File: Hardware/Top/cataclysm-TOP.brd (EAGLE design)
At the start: 160 x 100 mm, 0 parts

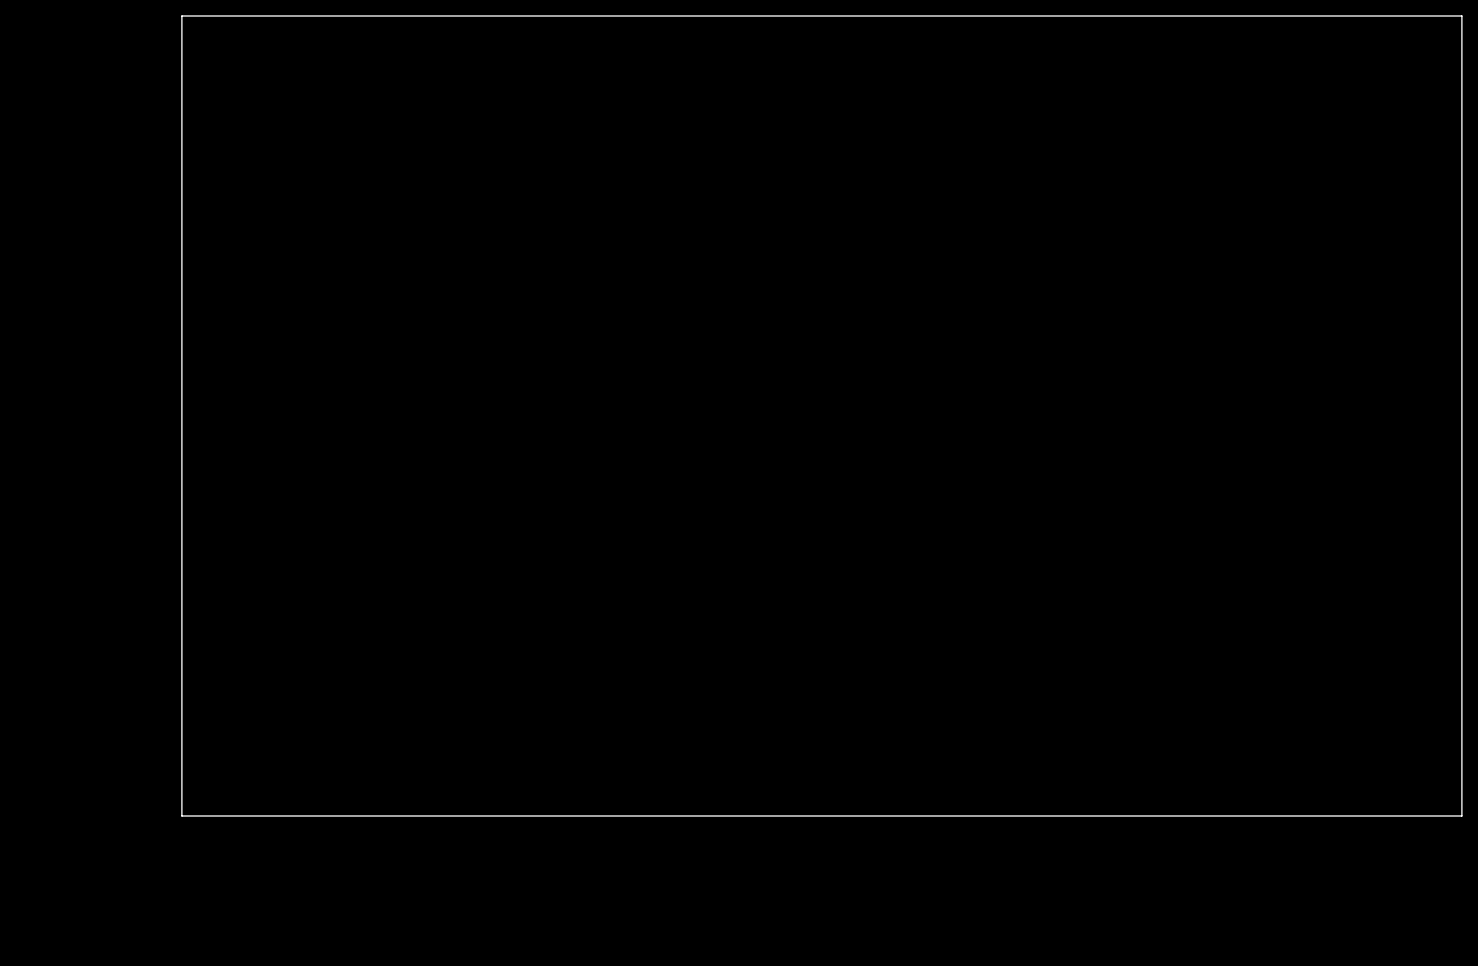
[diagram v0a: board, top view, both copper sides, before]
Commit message: Added OLED display, power management section, bluetooth microcontroller, and buttons
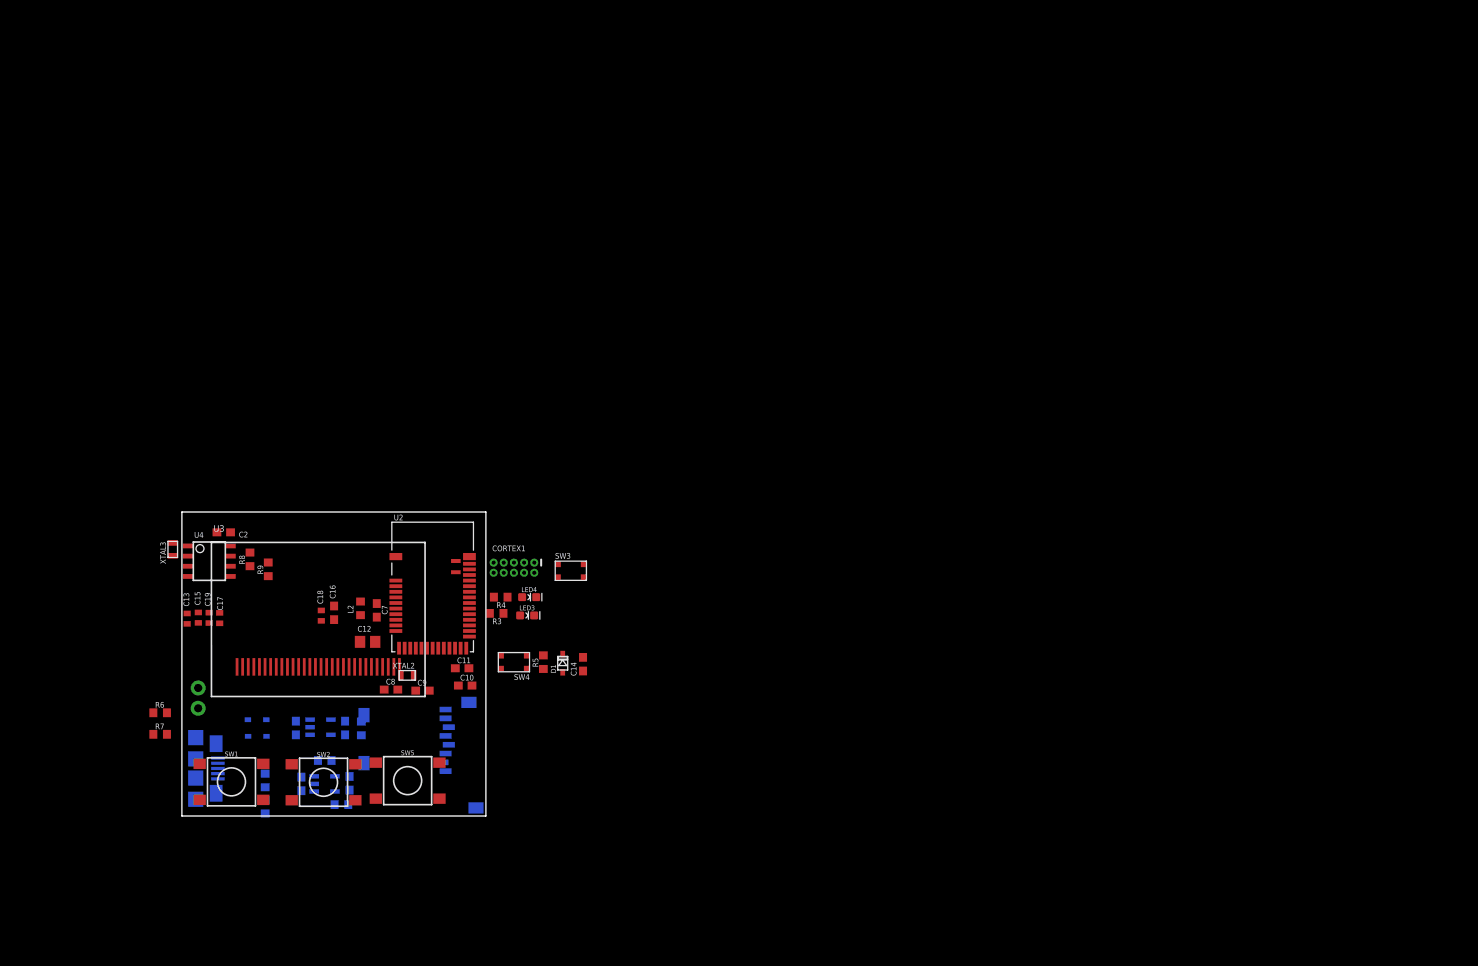
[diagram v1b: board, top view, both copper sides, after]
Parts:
- added C10, C11: 300p, LinnesLab-Passives:C0603
- added C12: 10u, LinnesLab-Passives:C0805
- added C13, C15, C17, C18, C19: 2.2uF, LinnesLab-Passives:C0402
- added C14: 100n, LinnesLab-Passives:C0603
- added C16: 10uF, LinnesLab-Passives:C0603
- added C2, C5, C6, C7: 1u, LinnesLab-Passives:C0603
- added C20, C21: 4.7u, LinnesLab-Passives:C0603
- added C8, C9: (no value), LinnesLab-Passives:C0603
- added CHRG2: MCP73831, LinnesLab-Power:SOT23-5
- added CORTEX1: CORTEX_DEBUG_PTH, LinnesLab-Connectors:2X5-PTH-1.27MM
- added D1, D4, D5: (no value), LinnesLab-DiscreteSemi:USC
- added J2: (no value), LinnesLab-Connectors:1X02
- added L2: 10u, LinnesLab-Passives:L0603
- added LDO2: MIC5504, LinnesLab-Power:SOT23-5
- added LED3: RED, LinnesLab-LED:LED-0603
- added LED4: BLUE, LinnesLab-LED:LED-0603
- added R11: (no value), LinnesLab-Passives:R0603
- added R12, R13, R14, R15: 100k, LinnesLab-Passives:R0603
- added R3, R4: 1k, LinnesLab-Passives:R0603
- added R5, R6, R8, R9: 10k, LinnesLab-Passives:R0603
- added R7: 390k, LinnesLab-Passives:R0603
- added SD3: (no value), LinnesLab-Connectors:MICROSD
- added SW1, SW2, SW5: SWITCH.MOM, LinnesLab-Switches:TACTILE_SWITCH_SMD_6.2MM_TALL
- added SW3, SW4: (no value), LinnesLab-Switches:BUTTON-GULLWING
- added U2: NRF52832_MODULE_MDBT42, LinnesLab-Microcontrollers:BLE_MODULE_RAYTAC_MDBT42
- added U3: (no value), LinnesLab-Displays:UG-2864HSWEG01_0.96IN_NO-WRAPAROUND
- added U4: PCF8523, LinnesLab-Clocks:SO8
- added USB2: USB.MICRO-BIGGERPADS, LinnesLab-Connectors:USB-MICRO-01.BIGGERPADS
- added XTAL2: 32.768kHz, LinnesLab-Clocks:2-SMD.NOLEAD.2.0MMTO1.2MM
- added XTAL3: 32.7680kHz, LinnesLab-Clocks:2-SMD.NOLEAD.2.0MMTO1.2MM
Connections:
- new net 3.3V: C12.2, C17.2, C19.2, C2.1, C6.1, CORTEX1.1, D1.-, LDO2.5, R15.2, R5.2, R8.2, R9.2, SD3.4, U2.11, U3.6, U3.9, U4.8
- new net BATT: R13.1, R14.2
- new net CD1: SD3.CD1
- new net CD2: SD3.CD2
- new net CHRG.STAT: CHRG2.1, R12.1
- new net CS.OLED: U3.13
- new net DC.OLED: U3.15
- new net DFU: SW3.3, U2.34
- new net DTR: C14.1
- new net FRST: U2.38
- new net GND: C10.2, C11.2, C12.1, C16.1, C17.1, C18.1, C19.1, C2.2, C20.2, C21.1, C5.1, C6.2, C7.2, C8.1, C9.2, CHRG2.2, CORTEX1.3, CORTEX1.5, CORTEX1.7, CORTEX1.9, J2.1, LDO2.2, LED3.C, LED4.C, R11.1, R14.1, R15.1, R6.1, R7.2, SD3.6, SD3.MT1, SD3.MT2, SW3.1, SW4.3, U2.1, U2.12, U2.24, U2.39, U3.1, U3.10, U3.12, U3.29, U3.30, U3.8, U4.4, USB2.5
- new net LED1: R3.2, U2.31
- new net LED2: R4.2, U2.33
- new net MISO: SD3.7, U2.28
- new net MOSI: SD3.3, U2.27, U3.19
- new net N$1: R6.2, U3.11
- new net N$10: LED4.A, R4.1
- new net N$11: L2.1, U2.10
- new net N$12: C7.1, L2.2, U2.9
- new net N$13: C16.2, U3.28
- new net N$14: CORTEX1.8
- new net N$15: C18.2, U3.27
- new net N$17: CHRG2.5, R11.2
- new net N$19: U4.2, XTAL3.P$1
- new net N$2: R7.1, U3.26
- new net N$20: U4.1, XTAL3.P$2
- new net N$3: C13.2, U3.2
- new net N$4: C8.2, U2.13, XTAL2.P$1
- new net N$5: C13.1, U3.3
- new net N$6: C9.1, U2.14, XTAL2.P$2
- new net N$7: C15.2, U3.4
- new net N$8: C15.1, U3.5
- new net N$9: LED3.A, R3.1
- new net P0.09/NFC1: C11.1, U2.22
- new net P0.10/NFC2: C10.1, U2.23
- new net RESET: C14.2, CORTEX1.10, D1.+, R5.1, SW4.1, U2.35
- new net RESET.OLED: U3.14
- new net RXD: U2.21
- new net SCK: SD3.5, U2.26, U3.18
- new net SCL: R8.1, U2.3, U4.6
- new net SD.CS: SD3.2
- new net SDA: R9.1, U2.2, U4.5
- new net SWCLK: CORTEX1.4, U2.36
- new net SWDIO: CORTEX1.2, U2.37
- new net SWO: CORTEX1.6, U2.32
- new net TXD: U2.19
- new net USB+: USB2.3
- new net USB-: USB2.2
- new net VBATT: U4.3
- new net VIN: C21.2, C5.2, CHRG2.4, D4.-, D5.-, LDO2.1, LDO2.3, R12.2
- new net VLIPO: C20.1, CHRG2.3, D4.+, J2.2, R13.2
- new net V_USB: D5.+, USB2.1
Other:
- board size 160 x 100 mm -> 38 x 38 mm

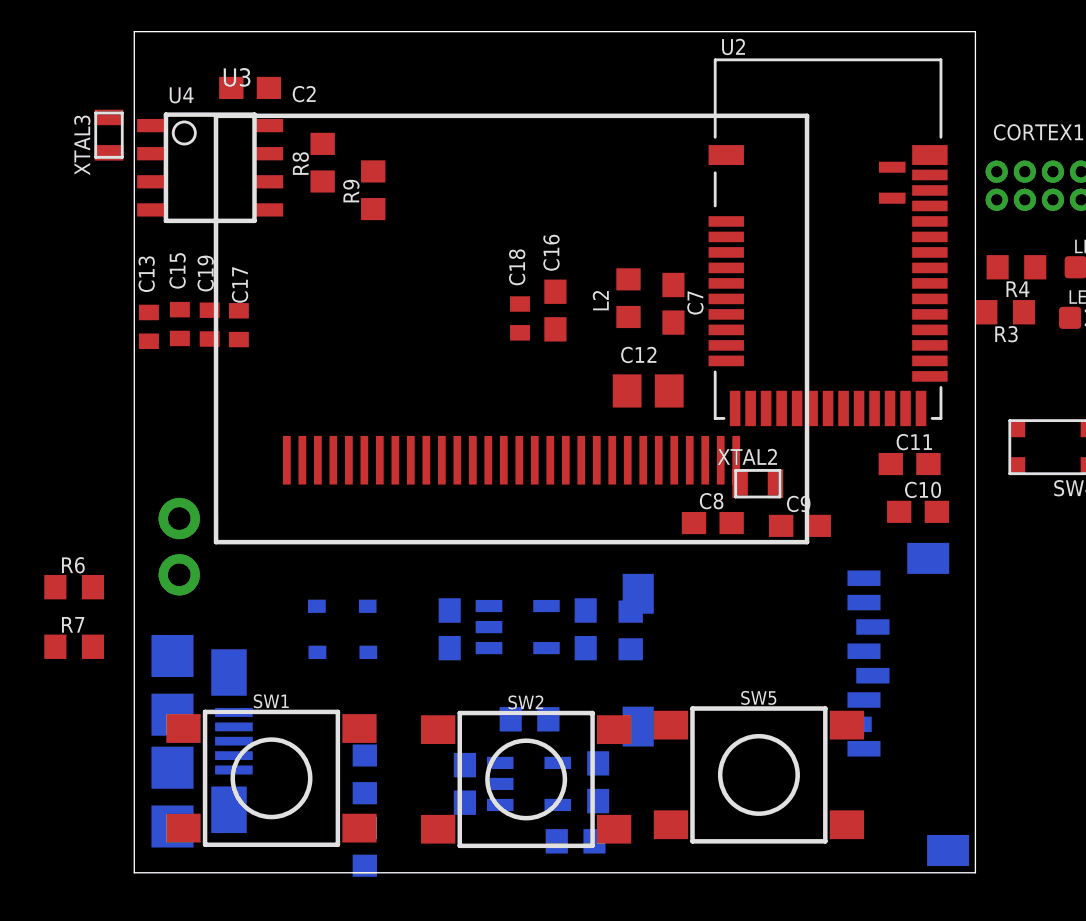
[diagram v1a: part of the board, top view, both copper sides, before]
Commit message: complete top circuit schematic
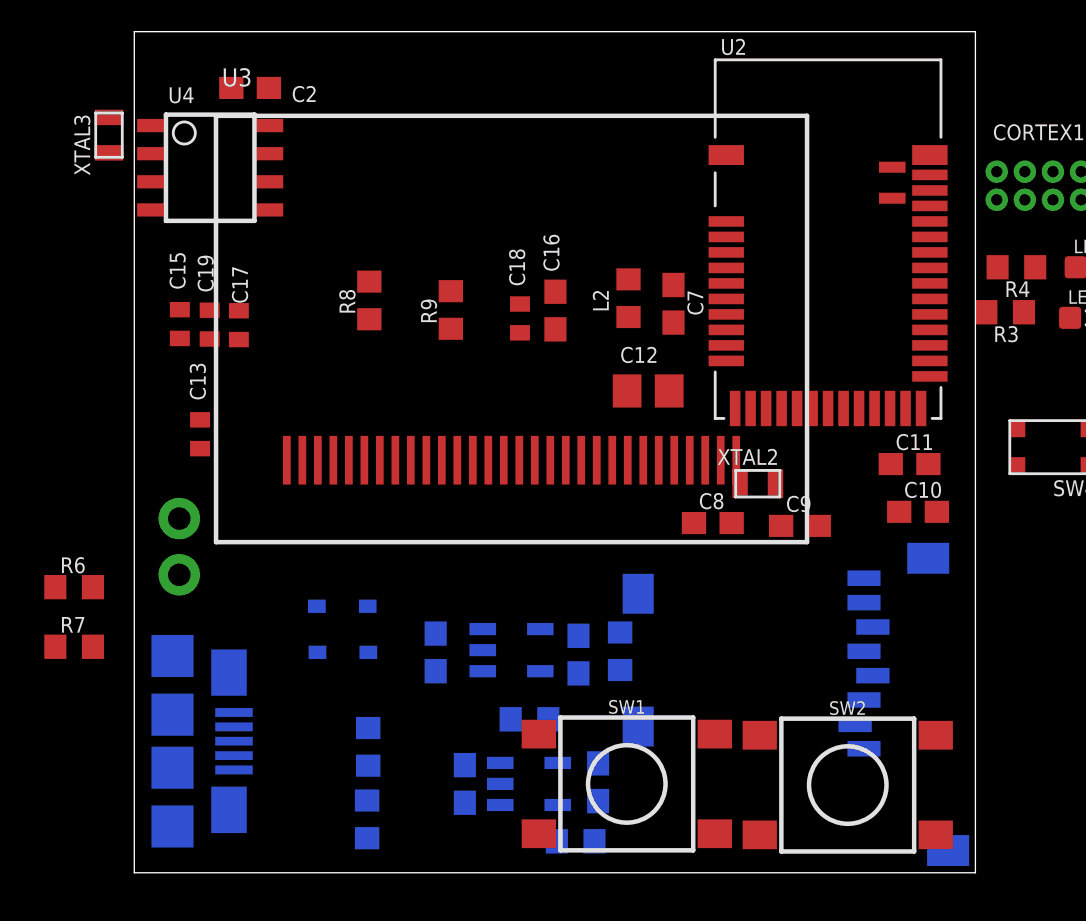
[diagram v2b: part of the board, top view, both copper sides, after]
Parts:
- removed SW5: SWITCH.MOM, LinnesLab-Switches:TACTILE_SWITCH_SMD_6.2MM_TALL
- moved SW1 16.1 mm to (22.3, 4.01)
- moved SW2 14.5 mm to (32.2, 3.96)
- moved R8 6.57 mm to (10.6, 25.9)
- moved R9 6.45 mm to (14.3, 25.4)
- moved C13 5.37 mm to (2.97, 19.8)
- moved R14 1.25 mm to (10.6, 5.69)
- moved R13 1.25 mm to (10.5, 2.41)
- moved C5 1.22 mm to (13.6, 9.96)
- moved C6 1.19 mm to (20.1, 9.86)
- moved LDO2 1.08 mm to (17.0, 10.1)
- moved R15 1.06 mm to (21.9, 10.0)
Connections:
- new net N$16: SW2.B2
- new net N$21: SW1.B2
- new net SW1: SW1.A1, SW2.A1
- net GND: now also SW1.B1, SW2.B1, USB2.S1, USB2.S2, USB2.S3, USB2.S4, USB2.S5, USB2.S6

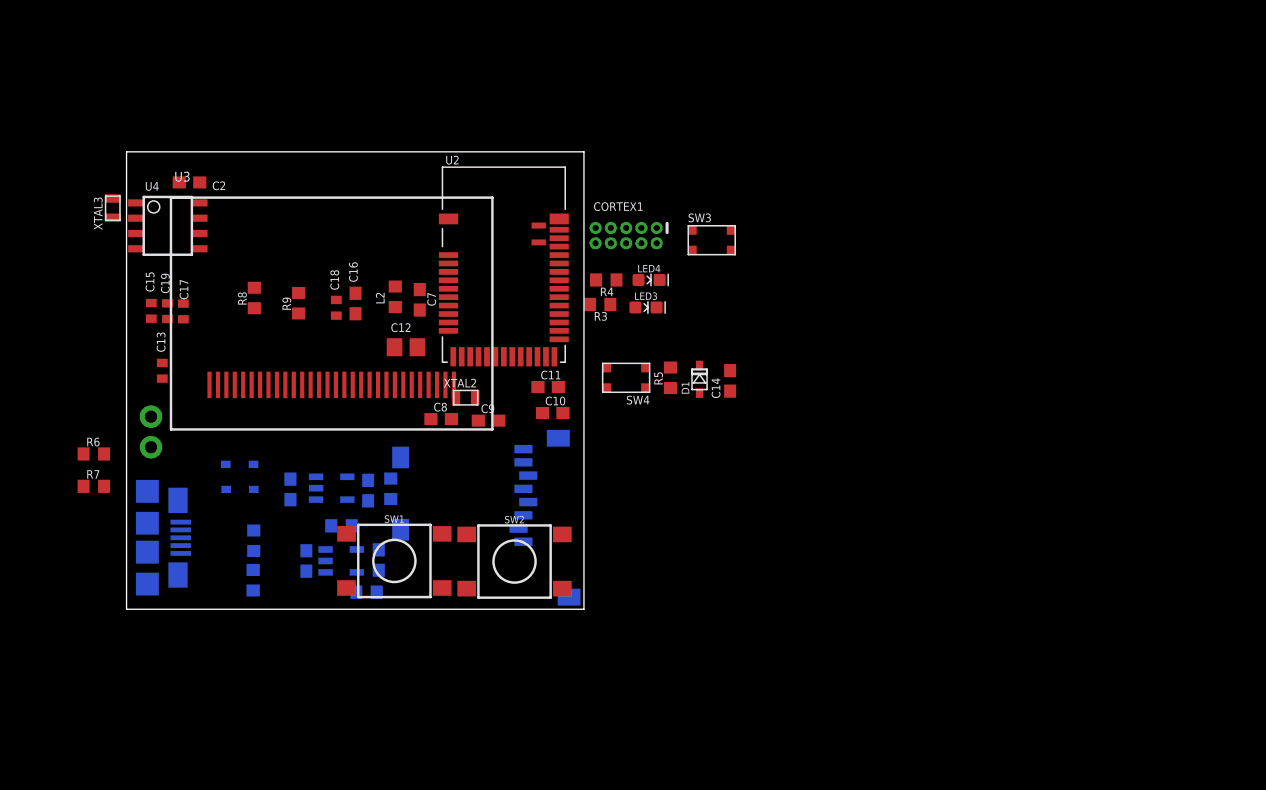
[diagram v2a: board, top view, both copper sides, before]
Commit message: Finished top and bottom schematic
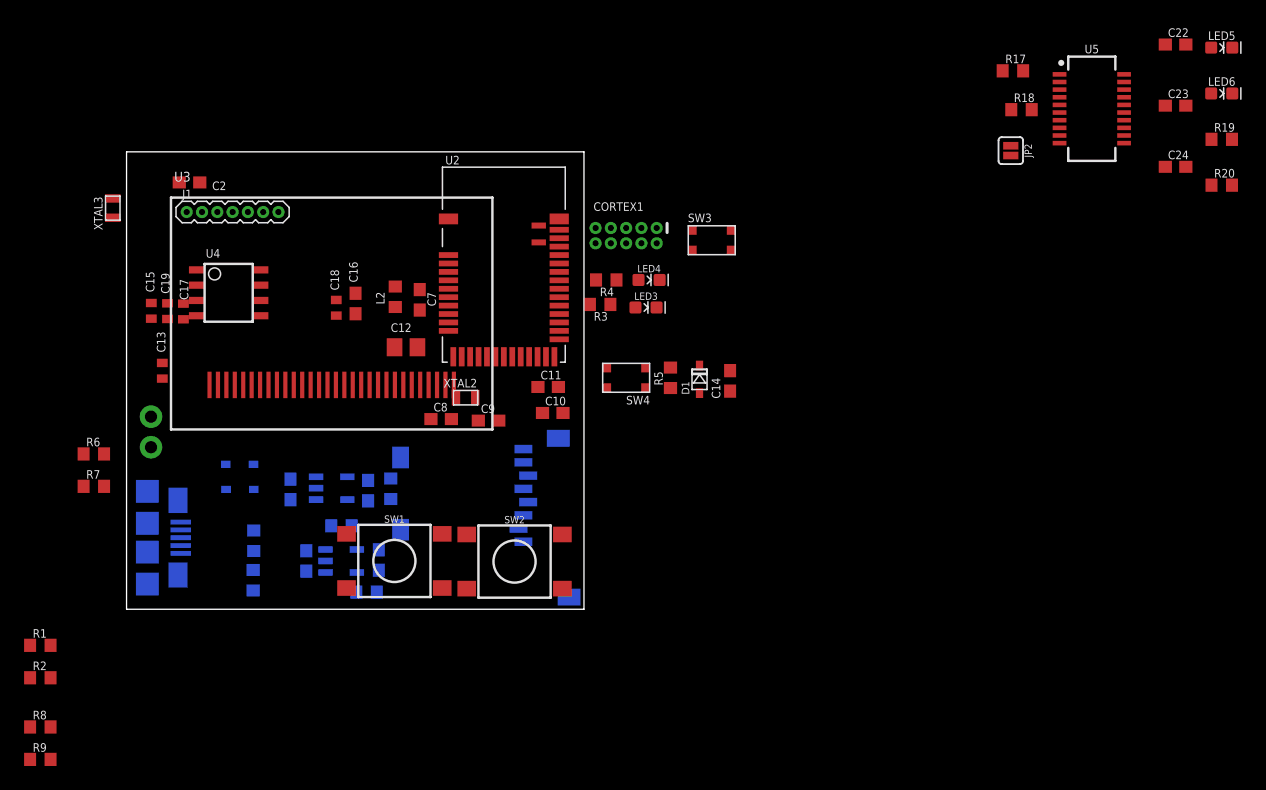
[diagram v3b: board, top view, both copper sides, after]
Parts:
- added C22: 100n, LinnesLab-Passives:C0603
- added C23, C24: 47p, LinnesLab-Passives:C0603
- added J1: (no value), LinnesLab-Connectors:1X07_1.27MM
- added JP2: (no value), LinnesLab-Switches:SMT-JUMPER_2_NO_SILK
- added LED5: RED, LinnesLab-LED:LED-0603
- added LED6: YELLOW, LinnesLab-LED:LED-0603
- added R1, R2: 0, LinnesLab-Passives:R0603
- added R17, R18: 27, LinnesLab-Passives:R0603
- added R19, R20: 1k, LinnesLab-Passives:R0603
- added U5: FT231XS, LinnesLab-DigitalIC:SSOP20_L
- moved R9 43.6 mm to (-7.16, -12.5), turned to 0 degrees
- moved R8 39.8 mm to (-7.16, -9.78), turned to 0 degrees
- moved U4 7.52 mm to (8.48, 26.3)
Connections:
- net VBATT renamed VBAT
- removed net BATT: R13.1, R14.2
- removed net CD1: SD3.CD1
- removed net CHRG.STAT: CHRG2.1, R12.1
- removed net CS.OLED: U3.13
- removed net DC.OLED: U3.15
- removed net RESET.OLED: U3.14
- removed net RXD: U2.21
- removed net SD.CS: SD3.2
- removed net SW1: SW1.A1, SW2.A1
- removed net TXD: U2.19
- new net !CTS: JP2.2, U5.9
- new net !DTR: U5.1
- new net A4/BATT: U2.5
- new net A6/TIA: U2.7
- new net A7/PPG: J1.7, U2.8
- new net A7/TIA: J1.5
- new net D11/SW1: SW1.A1, U2.25
- new net D15/SW2: SW2.A1, U2.29
- new net D16/CS.OLED: U2.30, U3.13
- new net D27/CHRG.STATUS: CHRG2.1, R12.1, R13.1, R14.2, U2.4
- new net D29/LED.CTRL: J1.6, U2.6
- new net D3/RESET.OLED: U2.17, U3.14
- new net D4/DC.OLED: U2.16, U3.15
- new net D7/SD.CS: SD3.2, U2.20
- new net DS/CD1: SD3.CD1, U2.18
- new net FT3V3: U5.13
- new net N$24: J1.4
- new net N$25: R17.2, U5.12
- new net N$26: R18.2, U5.11
- new net N$27: LED5.C, R19.2
- new net N$28: LED6.C, R20.2
- new net N$29: J1.3
- new net N$30: J1.2
- new net N$31: J1.1
- new net RXD.FT: R2.1, U5.4
- new net RXD.NRF: R1.2, U2.21
- new net RXLED: R19.1, U5.17
- new net TXD.FT: R1.1, U5.20
- new net TXD.NRF: R2.2, U2.19
- new net TXLED: R20.1, U5.10
- net 3.3V: now also C22.2, LED5.A, LED6.A, U5.14, U5.3
- net GND: now also C22.1, C23.2, C24.1, JP2.1, U5.16, U5.6
- net SCL: now also R9.1; no longer R8.1
- net SDA: now also R8.1; no longer R9.1
- net USB+: now also C23.1, R18.1
- net USB-: now also C24.2, R17.1
- net V_USB: now also U5.15
